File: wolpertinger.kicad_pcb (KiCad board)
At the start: 2 copper layers, 78.5 x 72.4 mm, 41 parts, among them IC1 TL074, IC2 TL074, K1 FRT5, K2 FRT5, Q1 BC549, T1 IN LEFT, T2 IN RIGHT, T3 SWT, T4 SWT, T5 OUT LEFT, T6 OUT RIGHT, T7 LED+, T8 LED-, U1 4093, U2 VTL5C, U3 VTL5C, U4 VTL5C, U5 VTL5C

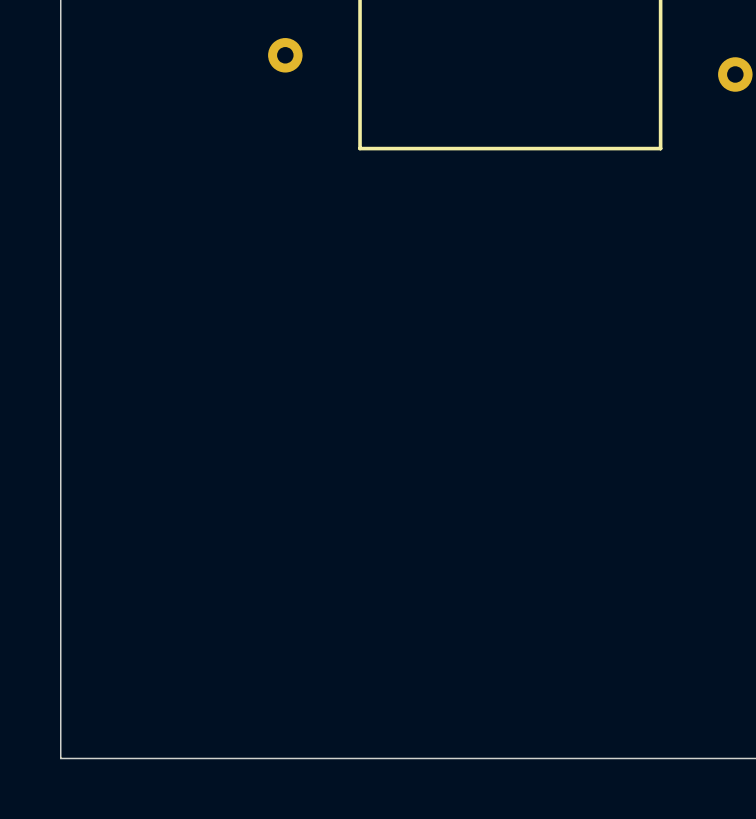
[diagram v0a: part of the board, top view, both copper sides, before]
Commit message: Add footprints
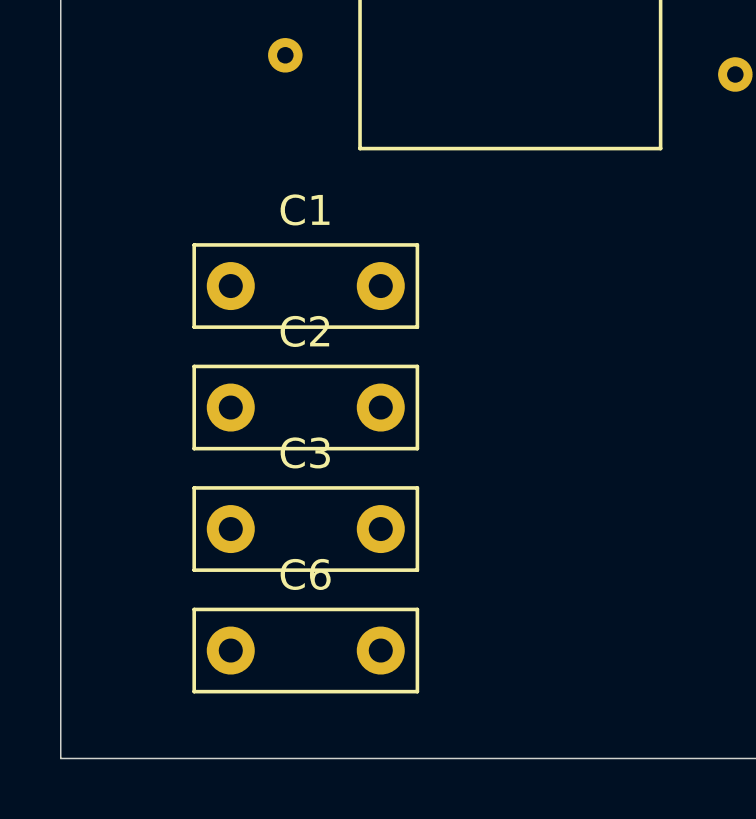
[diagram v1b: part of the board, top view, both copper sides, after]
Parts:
- added C1: 100nF, Capacitor_THT:C_Rect_L7.2mm_W2.5mm_P5.00mm_FKS2_FKP2_MKS2_MKP2, F.Cu at (-0.94, 20.8)
- added C2: 100nF, Capacitor_THT:C_Rect_L7.2mm_W2.5mm_P5.00mm_FKS2_FKP2_MKS2_MKP2, F.Cu at (-0.94, 24.9)
- added C3: 100nF, Capacitor_THT:C_Rect_L7.2mm_W2.5mm_P5.00mm_FKS2_FKP2_MKS2_MKP2, F.Cu at (-0.94, 28.9)
- added C6: 100nF, Capacitor_THT:C_Rect_L7.2mm_W2.5mm_P5.00mm_FKS2_FKP2_MKS2_MKP2, F.Cu at (-0.94, 33.0)

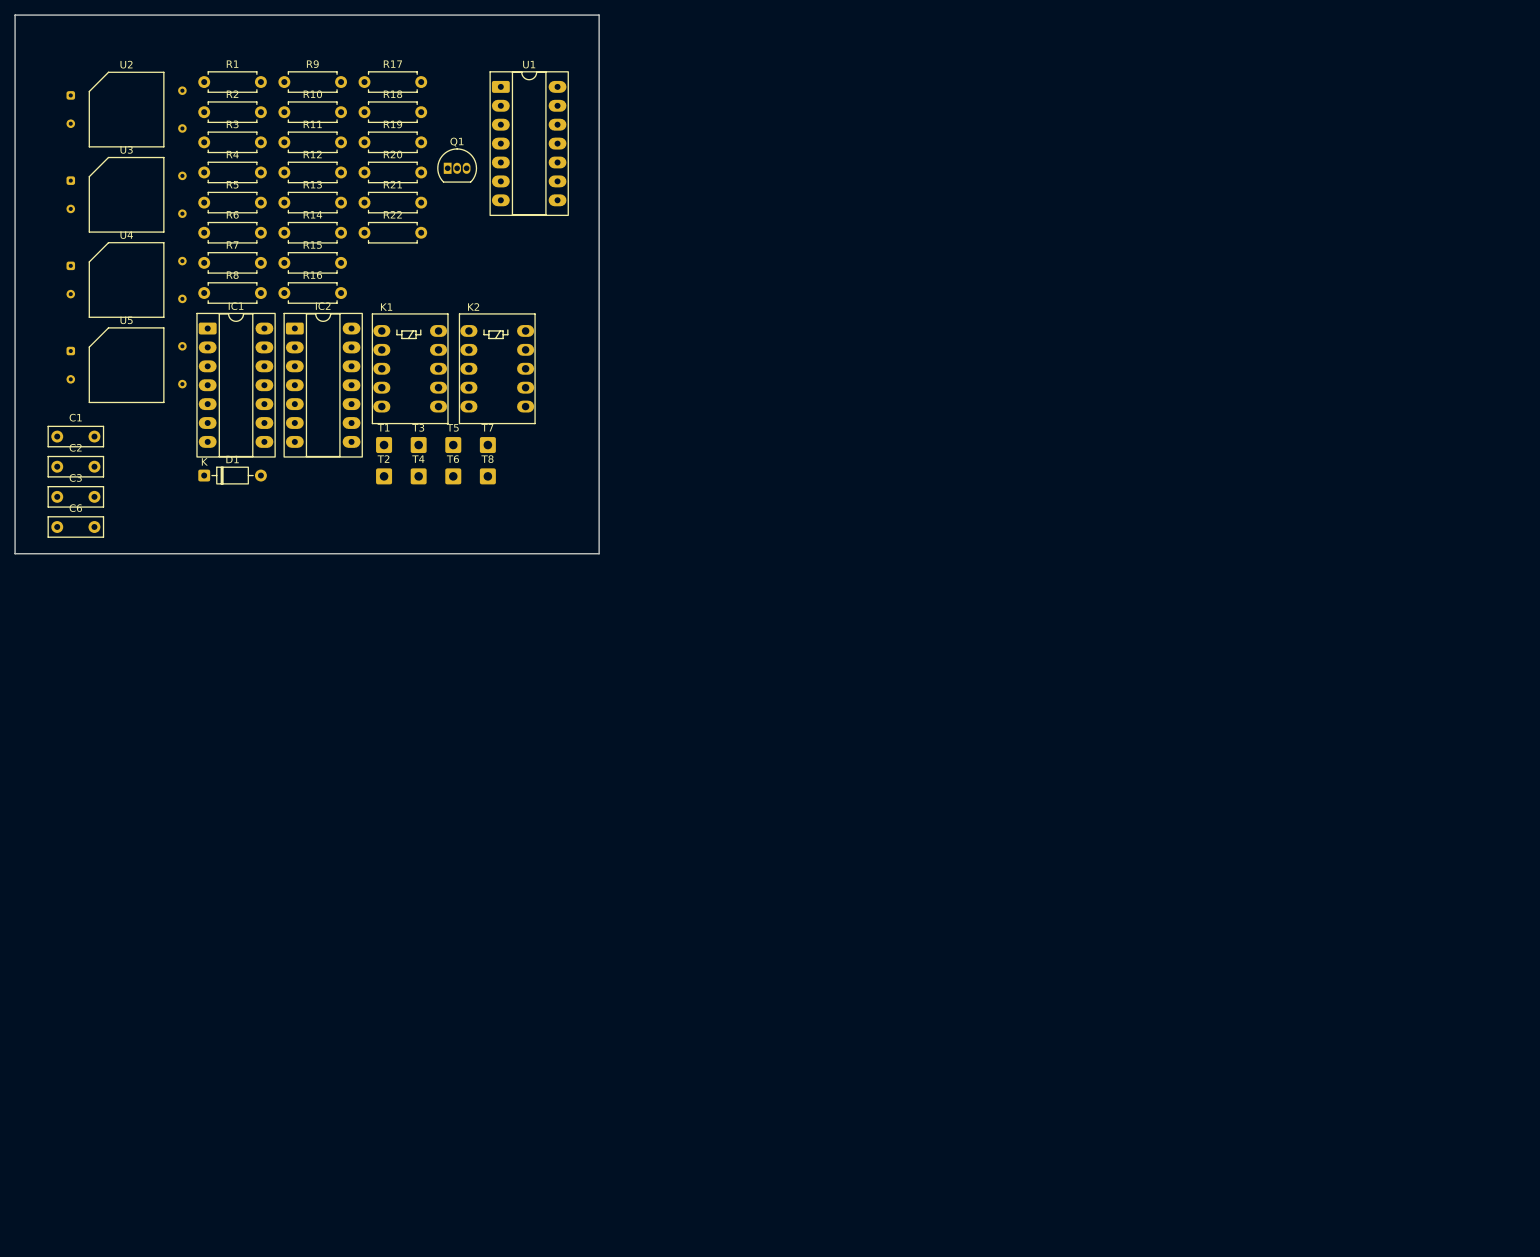
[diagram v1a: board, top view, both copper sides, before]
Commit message: add power supply
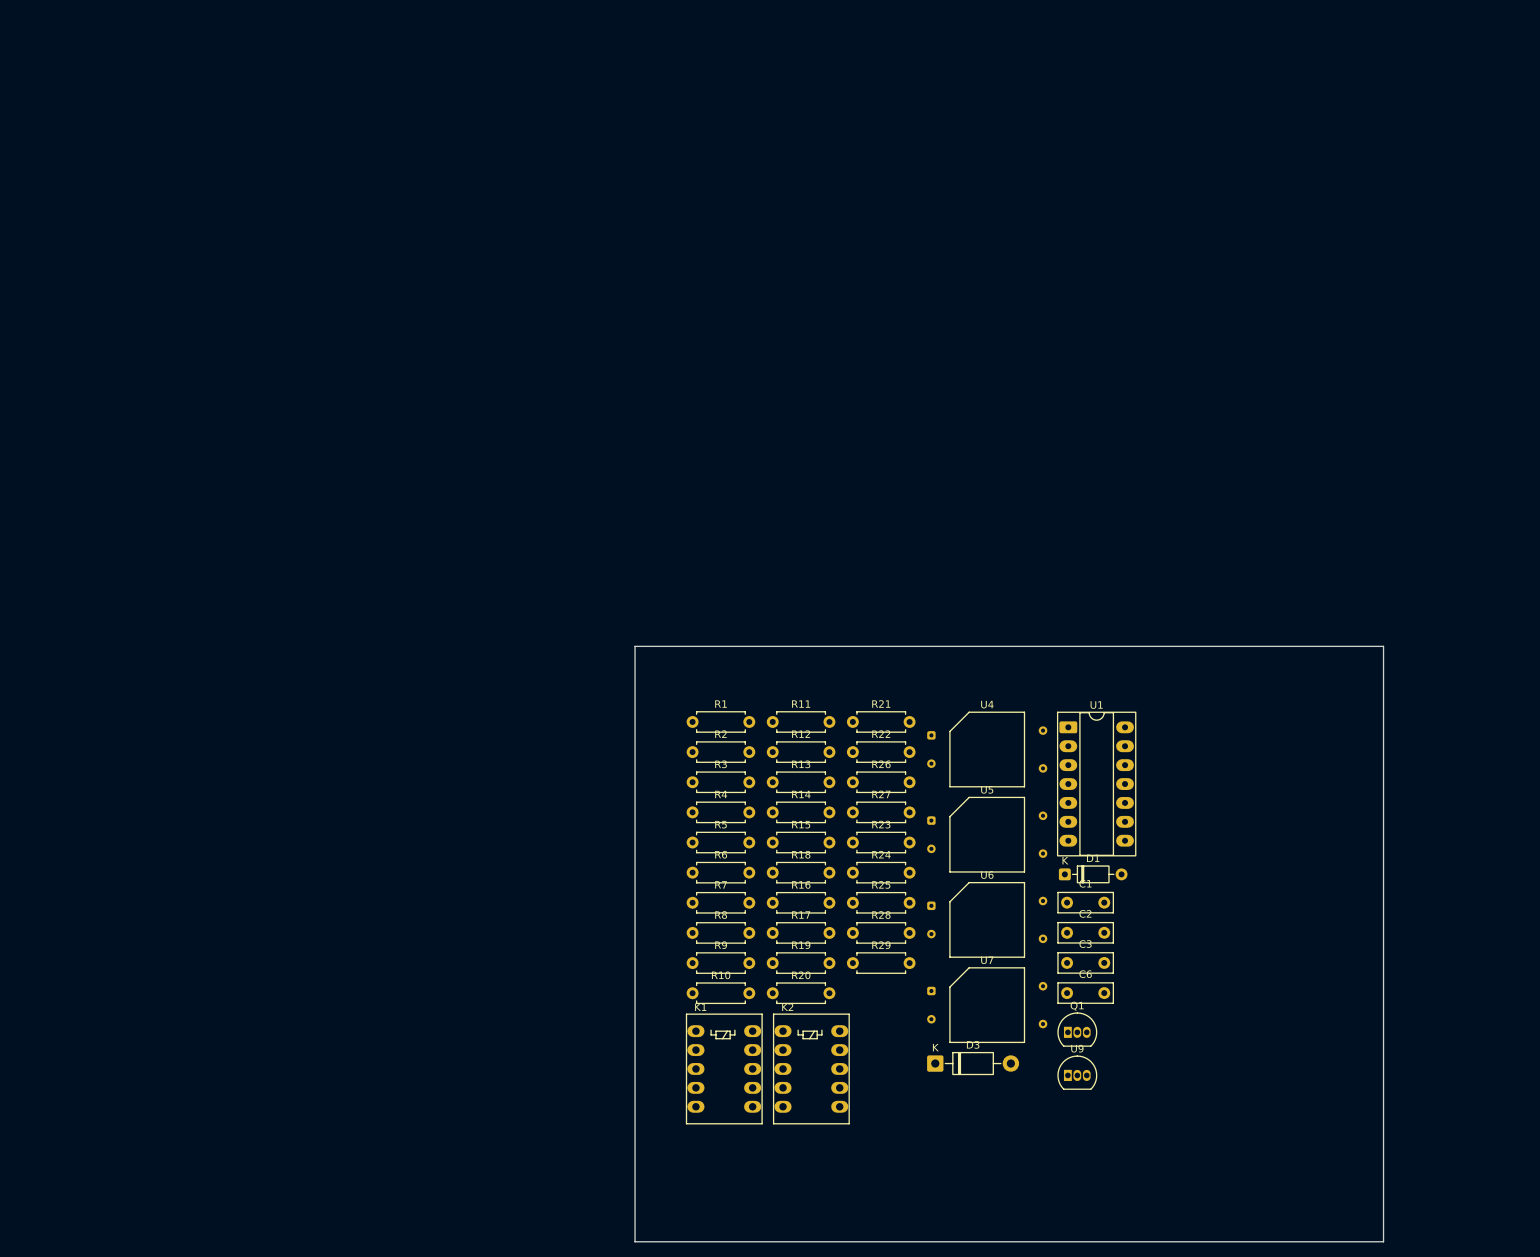
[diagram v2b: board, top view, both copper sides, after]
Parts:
- removed IC1, IC2: TL074, Package_DIP:CERDIP-14_W7.62mm_SideBrazed_LongPads_Socket
- removed T1: IN LEFT, Connector_Wire:SolderWire-0.5sqmm_1x01_D0.9mm_OD2.1mm
- removed T2: IN RIGHT, Connector_Wire:SolderWire-0.5sqmm_1x01_D0.9mm_OD2.1mm
- removed T3, T4: SWT, Connector_Wire:SolderWire-0.5sqmm_1x01_D0.9mm_OD2.1mm
- removed T5: OUT LEFT, Connector_Wire:SolderWire-0.5sqmm_1x01_D0.9mm_OD2.1mm
- removed T6: OUT RIGHT, Connector_Wire:SolderWire-0.5sqmm_1x01_D0.9mm_OD2.1mm
- removed T7: LED+, Connector_Wire:SolderWire-0.5sqmm_1x01_D0.9mm_OD2.1mm
- removed T8: LED-, Connector_Wire:SolderWire-0.5sqmm_1x01_D0.9mm_OD2.1mm
- removed U2, U3: VTL5C, OptoDevice:PerkinElmer_VTL5C
- added D3: 1N4001, Diode_THT:D_DO-41_SOD81_P10.16mm_Horizontal, F.Cu at (117.1, 105.1)
- added R23: 33r, Resistor_THT:R_Axial_DIN0207_L6.3mm_D2.5mm_P7.62mm_Horizontal, F.Cu at (106.0, 75.4)
- added R24: 33r, Resistor_THT:R_Axial_DIN0207_L6.3mm_D2.5mm_P7.62mm_Horizontal, F.Cu at (106.0, 79.4)
- added R25: 33r, Resistor_THT:R_Axial_DIN0207_L6.3mm_D2.5mm_P7.62mm_Horizontal, F.Cu at (106.0, 83.5)
- added R26: 100k, Resistor_THT:R_Axial_DIN0207_L6.3mm_D2.5mm_P7.62mm_Horizontal, F.Cu at (106.0, 67.3)
- added R27: 100k, Resistor_THT:R_Axial_DIN0207_L6.3mm_D2.5mm_P7.62mm_Horizontal, F.Cu at (106.0, 71.3)
- added R28: 100k, Resistor_THT:R_Axial_DIN0207_L6.3mm_D2.5mm_P7.62mm_Horizontal, F.Cu at (106.0, 87.5)
- added R29: 100k, Resistor_THT:R_Axial_DIN0207_L6.3mm_D2.5mm_P7.62mm_Horizontal, F.Cu at (106.0, 91.6)
- added U6: VTL5C, OptoDevice:PerkinElmer_VTL5C, F.Cu at (116.5, 83.9)
- added U7: VTL5C, OptoDevice:PerkinElmer_VTL5C, F.Cu at (116.5, 95.3)
- added U9: L78L05_TO92, Package_TO_SOT_THT:TO-92_Inline, F.Cu at (134.9, 106.7)
- moved C1 149.5 mm to (134.8, 83.5)
- moved C2 149.5 mm to (134.8, 87.5)
- moved C3 149.5 mm to (134.8, 91.6)
- moved C6 149.5 mm to (134.8, 95.6)
- moved Q1 142.9 mm to (134.9, 100.9)
- moved U5 131.7 mm to (116.5, 72.4)
- moved U4 131.7 mm to (116.5, 61.0)
- moved R9 130.5 mm to (84.4, 91.6)
- moved R10 130.5 mm to (84.4, 95.6)
- moved D1 127.5 mm to (134.5, 79.7)
- moved R17 126.8 mm to (95.2, 87.5)
- moved R19 123.2 mm to (95.2, 91.6)
- moved R20 123.2 mm to (95.2, 95.6)
- moved R18 116.0 mm to (95.2, 79.4)
- moved U1 115.0 mm to (134.9, 59.9)
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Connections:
- C1 pad 2: GND1 -> GND
- C6 pad 2: GND1 -> GND
- K1 pad 9: GND -> GND1
- K2 pad 9: GND -> GND2
- Q1 pad 3: GND1 -> GND
- R1 pad 2: GND -> GND1
- R11 pad 2: Net-(IC1C-+) -> Net-(U2B--)
- R12 pad 2: Net-(IC2B-+) -> Net-(U3C--)
- R13 pad 2: Net-(IC2C-+) -> Net-(U3B--)
- R16 pad 1: Net-(IC1-Pad8) -> Net-(U3C--)
- R16 pad 2: Net-(IC1C-+) -> Net-(C10-Pad2)
- R17 pad 1: Net-(IC2B-+) -> Net-(R17-Pad1)
- R17 pad 2: Net-(C10-Pad2) -> Net-(U3B--)
- R18 pad 2: Net-(IC2C-+) -> Net-(U2B--)
- R2 pad 2: GND -> GND2
- R20 pad 2: GND -> GND1
- R21 pad 2: GND -> GND2
- R4 pad 1: Vref1 -> Vref2
- U1 pad 12: GND1 -> GND
- U1 pad 13: GND1 -> GND
- U1 pad 7: GND1 -> GND
- U1 pad 8: GND1 -> GND
- U1 pad 9: GND1 -> GND
- U4 pad 3: Net-(C10-Pad2) -> Net-(C9-Pad2)
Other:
- board size 78.5 x 72.4 mm -> 100.6 x 80 mm

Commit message: add different power supply grounds
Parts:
- added D4: TBD, LED_THT:LED_D3.0mm, F.Cu at (135.1, 114.0)
- added JP1: ~, Jumper:SolderJumper-2_P1.3mm_Bridged_RoundedPad1.0x1.5mm, F.Cu at (92.5, 121.4)
- added JP2: ~, Jumper:SolderJumper-2_P1.3mm_Bridged_RoundedPad1.0x1.5mm, F.Cu at (108.3, 121.4)
- added JP3: ~, Jumper:SolderJumper-2_P1.3mm_Bridged_RoundedPad1.0x1.5mm, F.Cu at (127.3, 121.4)
- added U2: TL074, Package_DIP:CERDIP-14_W7.62mm_SideBrazed_LongPads_Socket, F.Cu at (146.5, 59.9)
- added U3: TL074, Package_DIP:CERDIP-14_W7.62mm_SideBrazed_LongPads_Socket, F.Cu at (158.2, 59.9)
- added U8: TL072, Package_DIP:DIP-8_W7.62mm_Socket_LongPads, F.Cu at (146.5, 80.0)
- moved R29 41.0 mm to (84.1, 126.2)
- moved R20 10.7 mm to (105.9, 95.8)

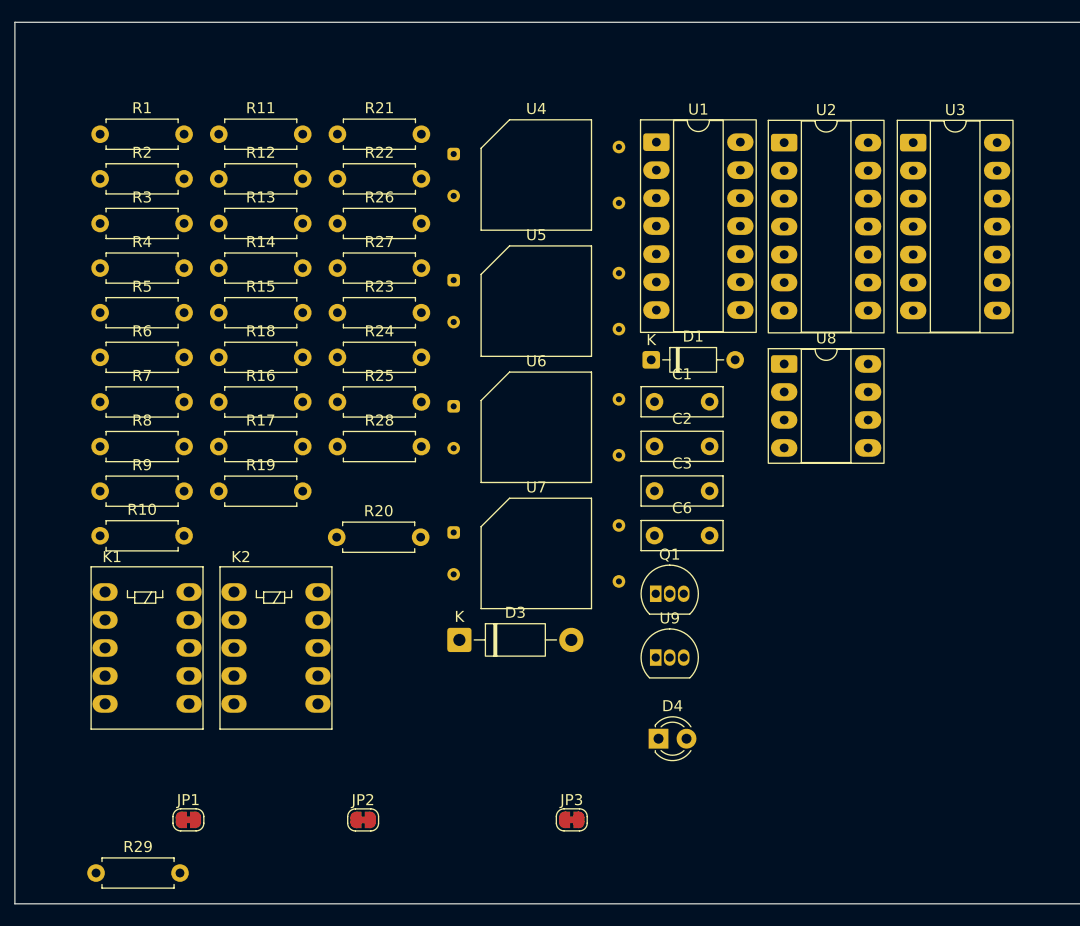
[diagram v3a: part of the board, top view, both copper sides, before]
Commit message: Add internal LFO
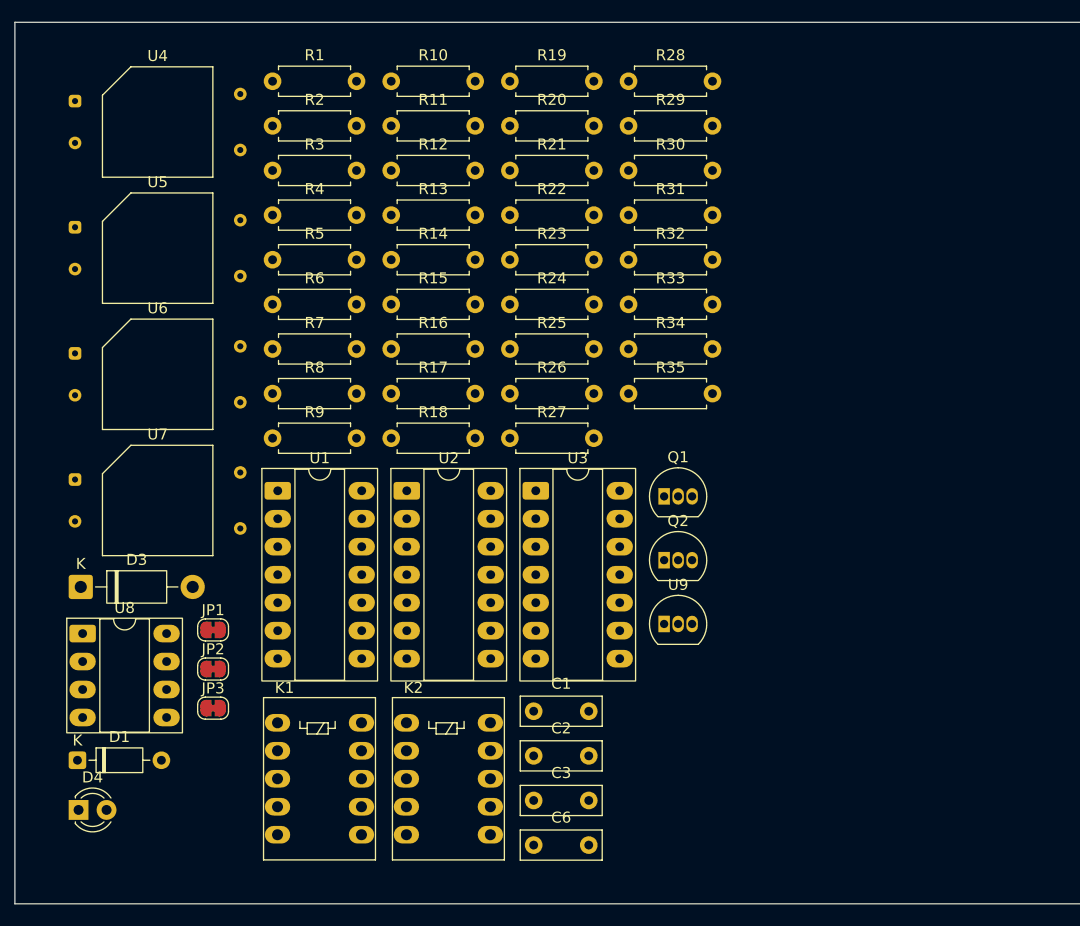
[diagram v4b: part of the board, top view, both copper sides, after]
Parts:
- added Q2: 2N5088, Package_TO_SOT_THT:TO-92_Inline, F.Cu at (135.6, 97.8)
- added R30: 33r, Resistor_THT:R_Axial_DIN0207_L6.3mm_D2.5mm_P7.62mm_Horizontal, F.Cu at (132.4, 62.5)
- added R31: 1k, Resistor_THT:R_Axial_DIN0207_L6.3mm_D2.5mm_P7.62mm_Horizontal, F.Cu at (132.4, 66.5)
- added R32: 100k, Resistor_THT:R_Axial_DIN0207_L6.3mm_D2.5mm_P7.62mm_Horizontal, F.Cu at (132.4, 70.6)
- added R33: 100k, Resistor_THT:R_Axial_DIN0207_L6.3mm_D2.5mm_P7.62mm_Horizontal, F.Cu at (132.4, 74.6)
- added R34: 100k, Resistor_THT:R_Axial_DIN0207_L6.3mm_D2.5mm_P7.62mm_Horizontal, F.Cu at (132.4, 78.7)
- added R35: 100k, Resistor_THT:R_Axial_DIN0207_L6.3mm_D2.5mm_P7.62mm_Horizontal, F.Cu at (132.4, 82.7)
- R23, R24: value 33r -> TBD
- R26: value 100k -> 33r
- R27, R29: value 100k -> 15k
- R28: value 100k -> 2M2
- moved R29 83.3 mm to (132.4, 58.4)
- moved U8 68.2 mm to (82.9, 104.5)
- moved D1 63.5 mm to (82.4, 116.0)
- moved D4 53.0 mm to (82.5, 120.5)
- moved R10 49.0 mm to (110.9, 54.4)
- moved U1 46.7 mm to (100.6, 91.5)
- moved U2 46.6 mm to (112.3, 91.5)
- moved U3 46.6 mm to (124.0, 91.5)
- moved R19 45.6 mm to (121.6, 54.4)
- moved R28 42.4 mm to (132.4, 54.4)
- moved R20 40.5 mm to (121.6, 58.4)
- moved U5 34.7 mm to (82.2, 67.6)
- moved U4 34.7 mm to (82.2, 56.2)
- moved U6 34.7 mm to (82.2, 79.1)
- moved U7 34.7 mm to (82.2, 90.5)
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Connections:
- R23 pad 1: Net-(D3-K) -> Net-(C13-Pad2)
- R23 pad 2: Net-(U3E-V+) -> LFO
- R24 pad 1: Net-(D3-K) -> LFO
- R24 pad 2: Net-(U2E-V+) -> GND3
- R25 pad 2: Net-(U9-VI) -> Net-(U3E-V+)
- R26 pad 1: Net-(U3E-V+) -> Net-(D3-K)
- R26 pad 2: Net-(U8A-+) -> Net-(U2E-V+)
- R27 pad 1: Net-(U8A-+) -> V3
- R27 pad 2: GND1 -> Net-(Q2-C)
- R28 pad 1: V3 -> Net-(Q2-C)
- R28 pad 2: Vref 3 -> Net-(Q2-B)
- R29 pad 1: Vref 3 -> Net-(C18-Pad2)
